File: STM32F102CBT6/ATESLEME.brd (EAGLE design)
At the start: 35.3 x 57.9 mm, 55 parts, among them U1 ADXL345PATRICK, U3 AMS1117-3.3, U4 STM32F102CBT6, Y2 ABM2B-8.000MHZ-10-1-U-T

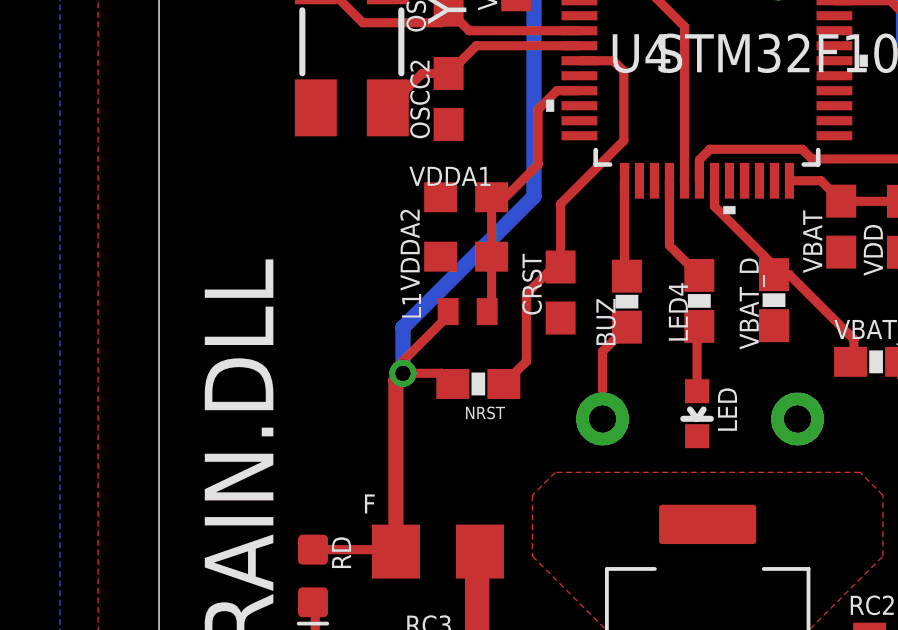
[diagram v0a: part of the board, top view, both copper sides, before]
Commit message: packages was modified according to stock situation
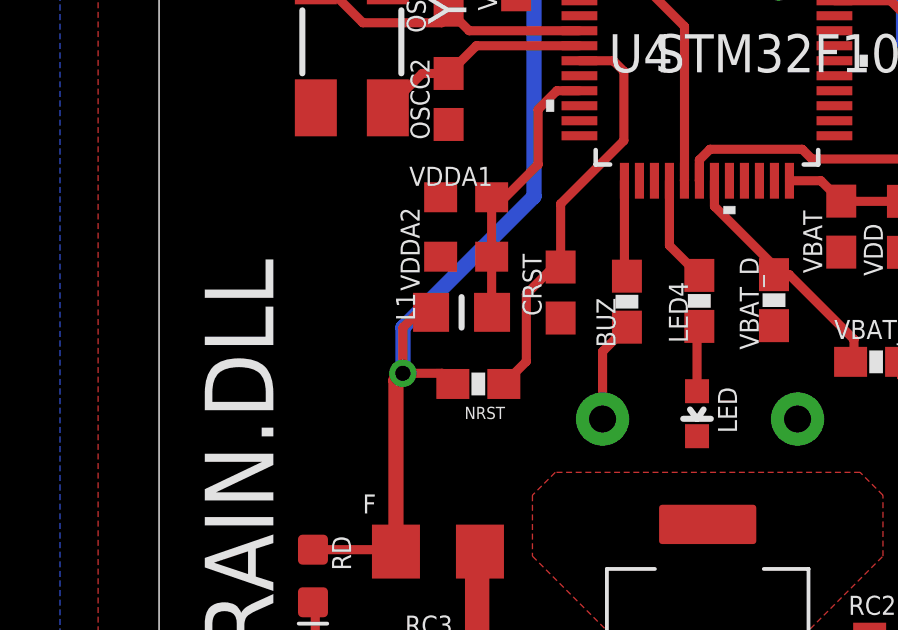
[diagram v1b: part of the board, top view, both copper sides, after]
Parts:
- G1, G2: value 20 -> 22
- L1: value BLM15HB221SN1 -> (none); device inductors:0402 -> 52101-101-REV-A_v16:RC-MASTER-SMD_L0805MP
- moved L1 0.20 mm to (3.91, 29.8)
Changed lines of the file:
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@@
 <drawing>
 <settings>
-<setting alwaysvectorfont="yes"/>
+<setting alwaysvectorfont="no"/>
 <setting verticaltext="up"/>
 </settings>
@@
 <attribute name="VALUE" x="4.6482" y="19.939" size="0.635" layer="27" font="vector" ratio="15" rot="R180" align="top-center"/>
 </element>
-<element name="G1" library="SparkFun-Resistors" package="0603-RES" value="20" x="17.3456625" y="54.366159375" smashed="yes" rot="R270">
+<element name="G1" library="SparkFun-Resistors" package="0603-RES" value="22" x="17.3456625" y="54.366159375" smashed="yes" rot="R270">
 <attribute name="NAME" x="16.398240625" y="55.8774625" size="0.635" layer="25" font="vector" ratio="15"/>
 <attribute name="PROD_ID" value="RES-08296" x="-33.4543375" y="12.456159375" size="1.778" layer="27" rot="R270" display="off"/>
 <attribute name="VALUE" x="18.628359375" y="52.6567375" size="0.635" layer="27" font="vector" ratio="15" rot="R180"/>
 </element>
-<element name="G2" library="SparkFun-Resistors" package="0603-RES" value="20" x="2.0574" y="51.4858" smashed="yes">
+<element name="G2" library="SparkFun-Resistors" package="0603-RES" value="22" x="2.0574" y="51.4858" smashed="yes">
 <attribute name="NAME" x="0.6604" y="52.2478" size="0.635" layer="25" font="vector" ratio="15"/>
 <attribute name="PROD_ID" value="RES-08296" x="47.7774" y="0.6858" size="1.778" layer="27" display="off"/>
 <attribute name="VALUE" x="2.5654" y="50.0888" size="0.635" layer="27" font="vector" ratio="15"/>
 </element>
-<element name="L1" library="inductors" library_urn="urn:adsk.eagle:library:243" package="0402" package3d_urn="urn:adsk.eagle:package:15132/1" value="BLM15HB221SN1" x="4.1148" y="29.845" smashed="yes">
-<attribute name="NAME" x="2.5654" y="29.5656" size="0.635" layer="25" font="vector" ratio="15" rot="R90"/>
-<attribute name="POPULARITY" value="0" x="49.8348" y="-6.985" size="1.778" layer="27" display="off"/>
+<element name="L1" library="52101-101-REV-A_v16" library_urn="urn:adsk.eagle:library:21899384" package="RC-MASTER-SMD_L0805MP" package3d_urn="urn:adsk.eagle:package:15662270/2" value="" x="3.9116" y="29.8196" smashed="yes">
+<attribute name="NAME" x="2.3622" y="29.5402" size="0.635" layer="25" font="vector" ratio="15" rot="R90"/>
 </element>
 <element name="LED" library="SparkFun-LED" package="LED-0603" value="GREEN" x="11.7602" y="26.4414" smashed="yes" rot="R180">
@@
 <wire x1="1.9558" y1="27.7876" x2="1.7242" y2="27.556" width="0.508" layer="1"/>
 <wire x1="1.7242" y1="27.556" x2="1.7242" y2="21.844" width="0.508" layer="1"/>
-<wire x1="3.4648" y1="29.703" x2="3.4648" y2="29.845" width="0.508" layer="1"/>
 <via x="1.9558" y="27.7876" extent="1-16" drill="0.508"/>
 <wire x1="6.3246" y1="33.6804" x2="1.9558" y2="29.3116" width="0.508" layer="16"/>
@@
 <wire x1="15.34921875" y1="50.48408125" x2="15.34921875" y2="50.23154375" width="0.3048" layer="1"/>
 <wire x1="14.8376" y1="49.483196875" x2="15.34921875" y2="49.994815625" width="0.3048" layer="1"/>
-<wire x1="1.9558" y1="27.7876" x2="1.9558" y2="28.194" width="0.3048" layer="1"/>
-<wire x1="1.9558" y1="28.194" x2="3.4648" y2="29.703" width="0.3048" layer="1"/>
+<wire x1="1.9558" y1="27.7876" x2="1.9558" y2="29.3116" width="0.3048" layer="1"/>
+<wire x1="2.8956" y1="29.8196" x2="2.4638" y2="29.8196" width="0.3048" layer="1"/>
+<wire x1="2.4638" y1="29.8196" x2="1.9558" y2="29.3116" width="0.3048" layer="1"/>
 <wire x1="6.3246" y1="42.181778125" x2="7.25931875" y2="42.181778125" width="0.3048" layer="16"/>
 <via x="7.25931875" y="42.181778125" extent="1-16" drill="0.4064"/>
@@
 <wire x1="5.3712" y1="33.655" x2="4.914" y2="33.655" width="0.2286" layer="1"/>
 <wire x1="4.914" y1="33.655" x2="4.914" y2="31.6738" width="0.3048" layer="1"/>
-<wire x1="4.914" y1="31.6738" x2="4.914" y2="29.9942" width="0.3048" layer="1"/>
-<wire x1="4.7648" y1="29.845" x2="4.914" y2="29.9942" width="0.2286" layer="1"/>
+<wire x1="4.914" y1="31.6738" x2="4.914" y2="29.828959375" width="0.3048" layer="1"/>
+<wire x1="4.9276" y1="29.8196" x2="4.914" y2="29.828959375" width="0.2286" layer="1"/>
 <contactref element="U4" pad="9"/>
 <wire x1="7.08693125" y1="37.2056" x2="7.8404" y2="37.2056" width="0.3048" layer="1"/>
